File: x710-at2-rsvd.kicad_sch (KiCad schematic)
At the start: 37 parts, among them U1 EZX710AT2_S_LMR5

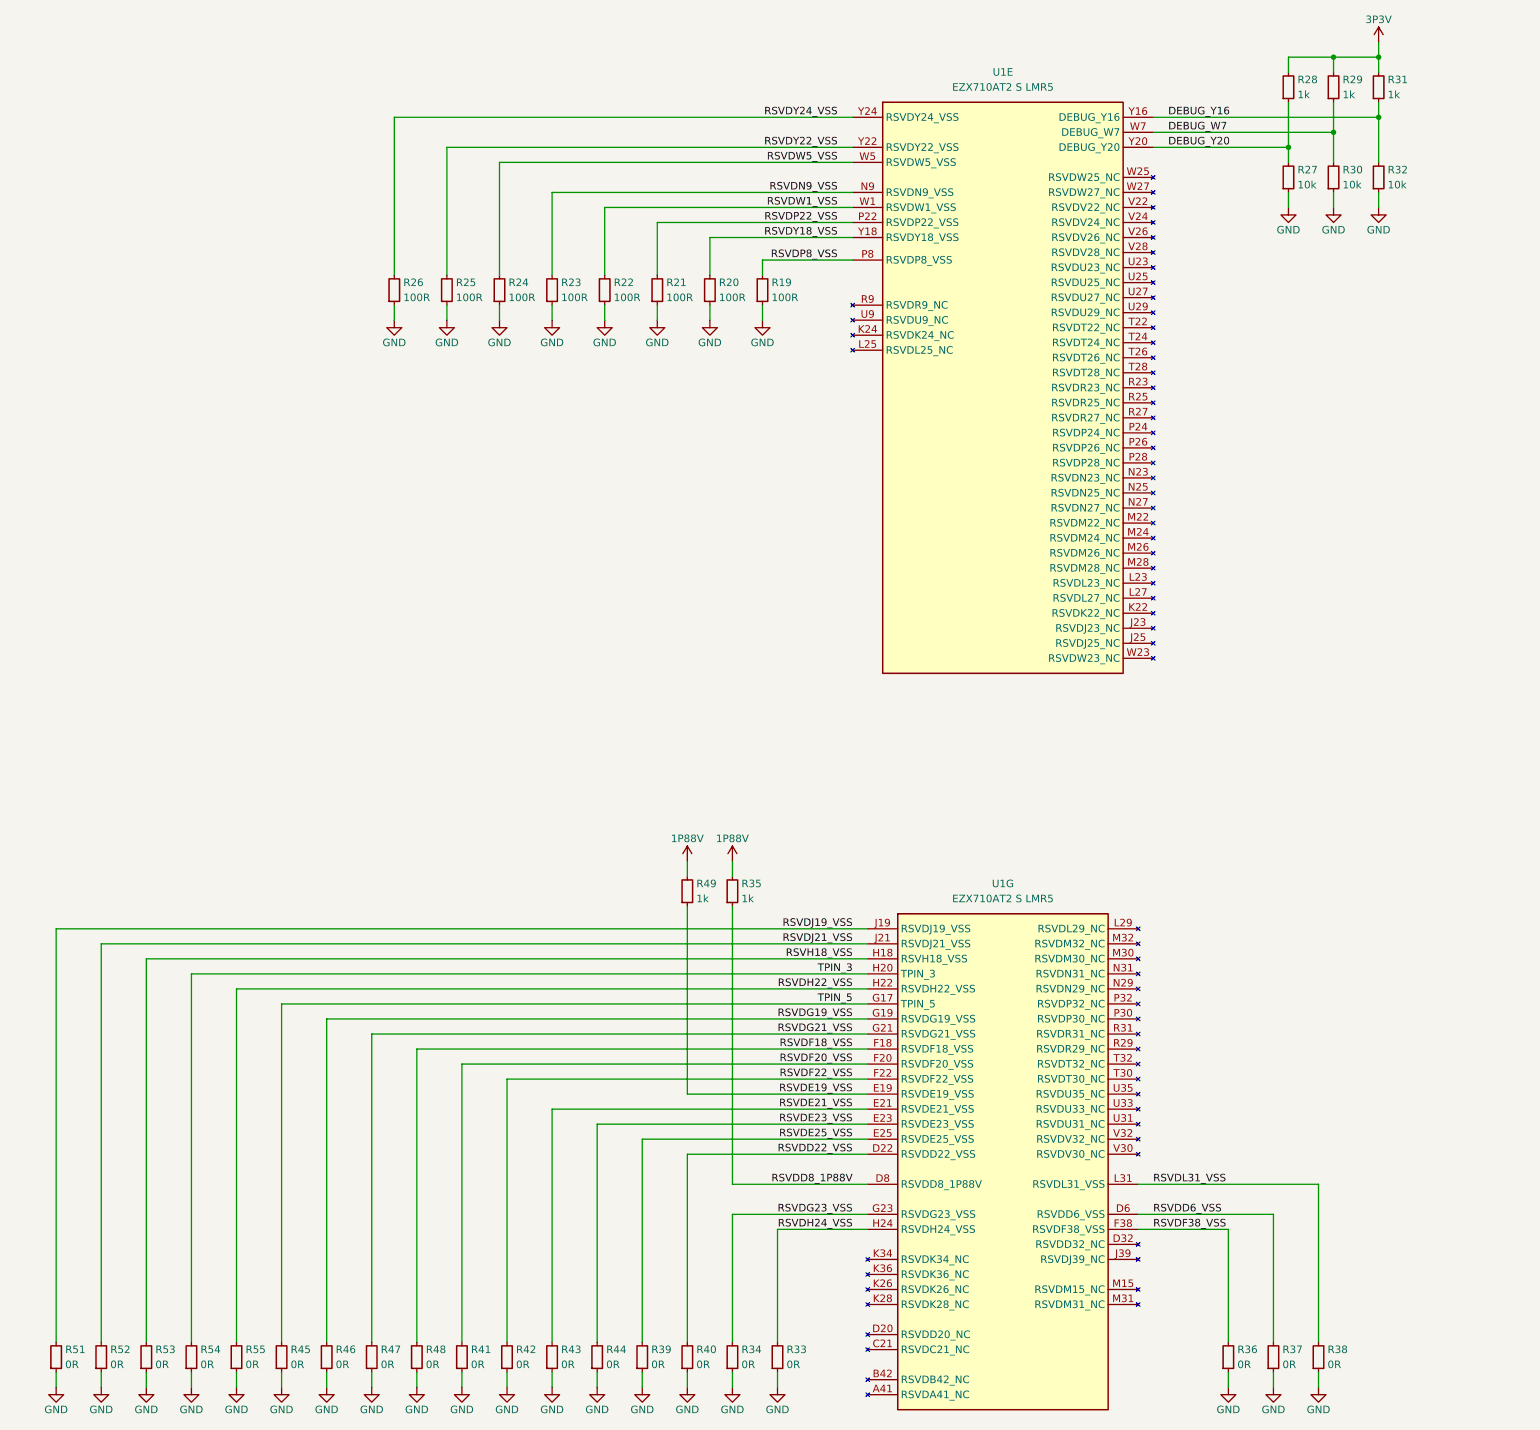
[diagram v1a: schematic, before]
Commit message: [#80813] Change RJ45 connectors, reannotate schematics
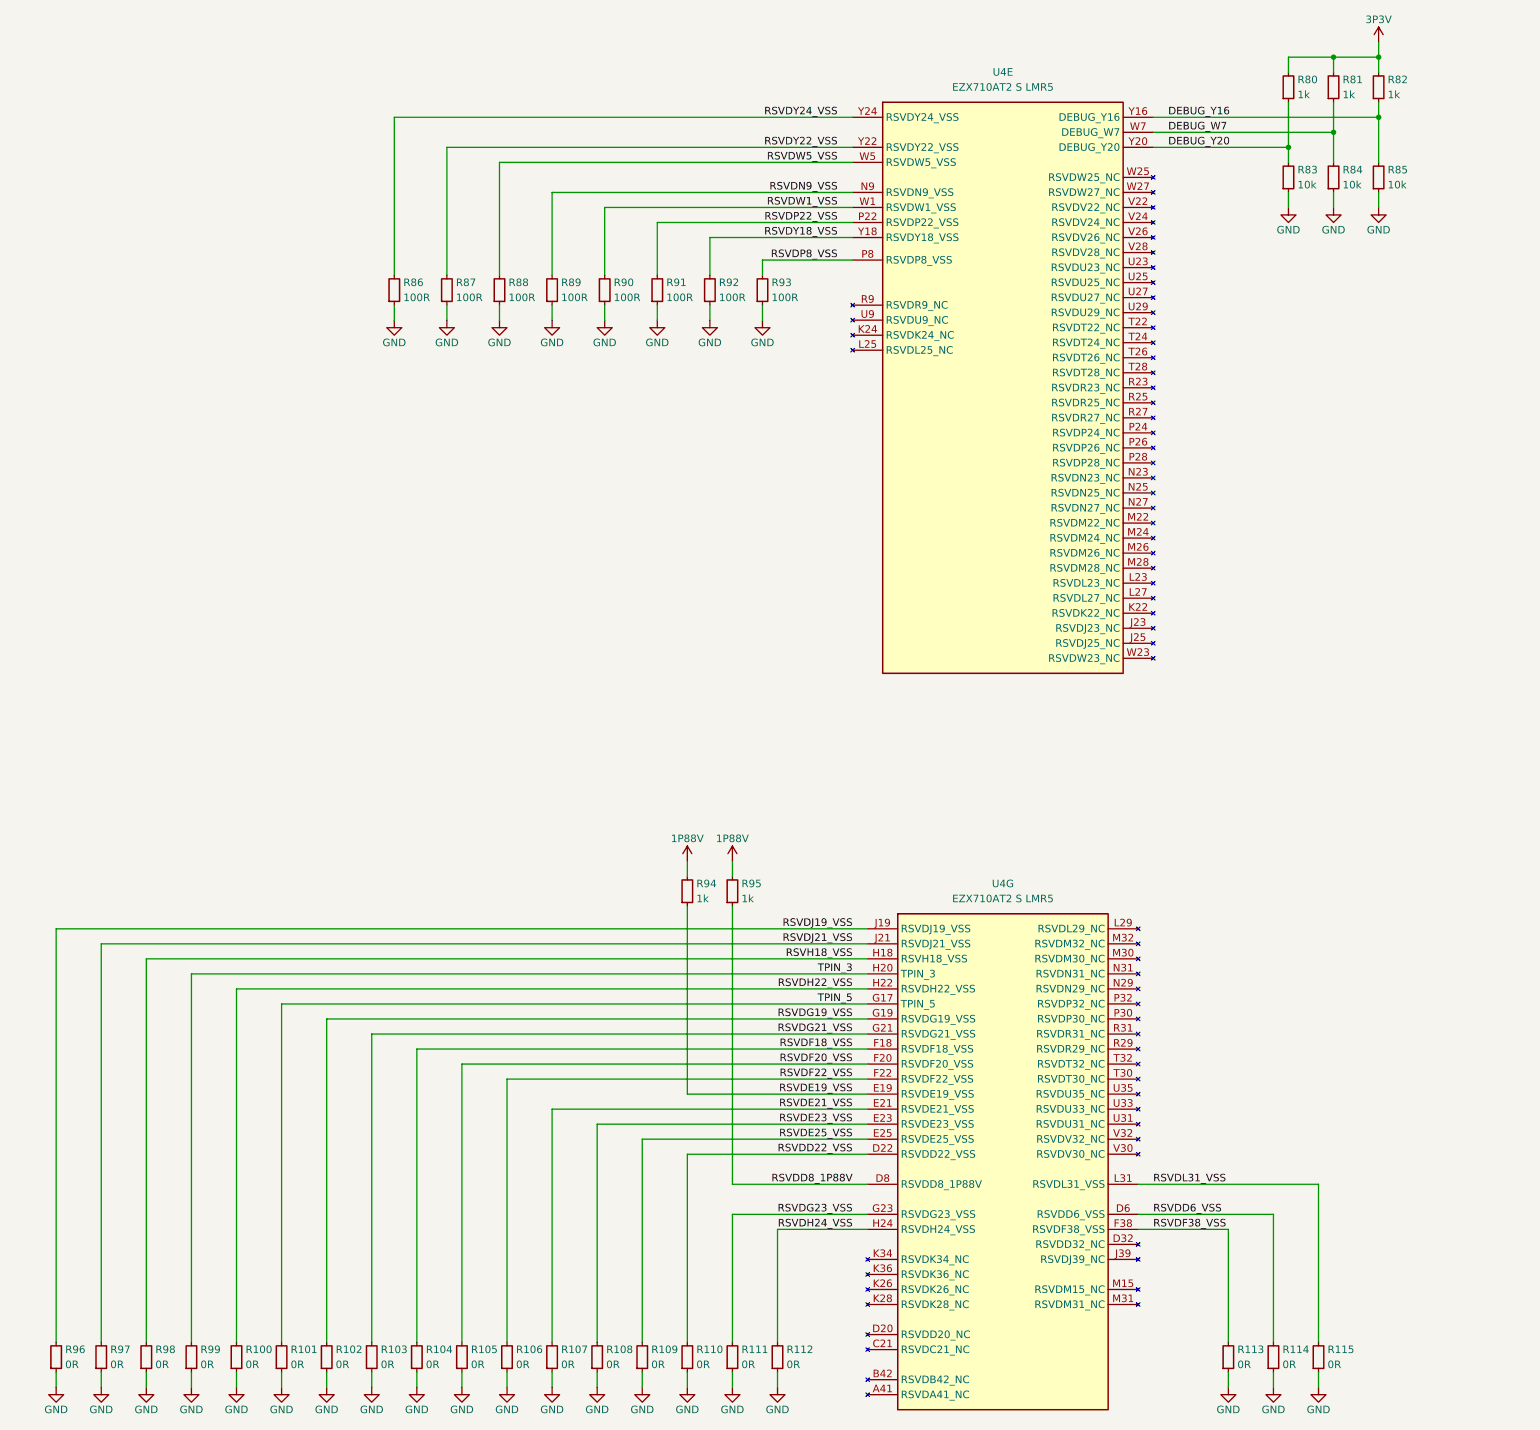
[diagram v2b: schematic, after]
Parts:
- renumbered R55 to R100, R45 to R101, R46 to R102, R47 to R103, R48 to R104, R41 to R105, R42 to R106, R43 to R107, R44 to R108, R39 to R109, R40 to R110, R34 to R111, R33 to R112, R36 to R113, R37 to R114, R38 to R115, R28 to R80, R29 to R81, R31 to R82, R27 to R83, R30 to R84, R32 to R85, R26 to R86, R25 to R87, R24 to R88, R23 to R89, R22 to R90, R21 to R91, R20 to R92, R19 to R93, R49 to R94, R35 to R95, R51 to R96, R52 to R97, R53 to R98, R54 to R99, U1 to U4

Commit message: [#80813] Improve schematic readability, add debug connectors and missing resistors
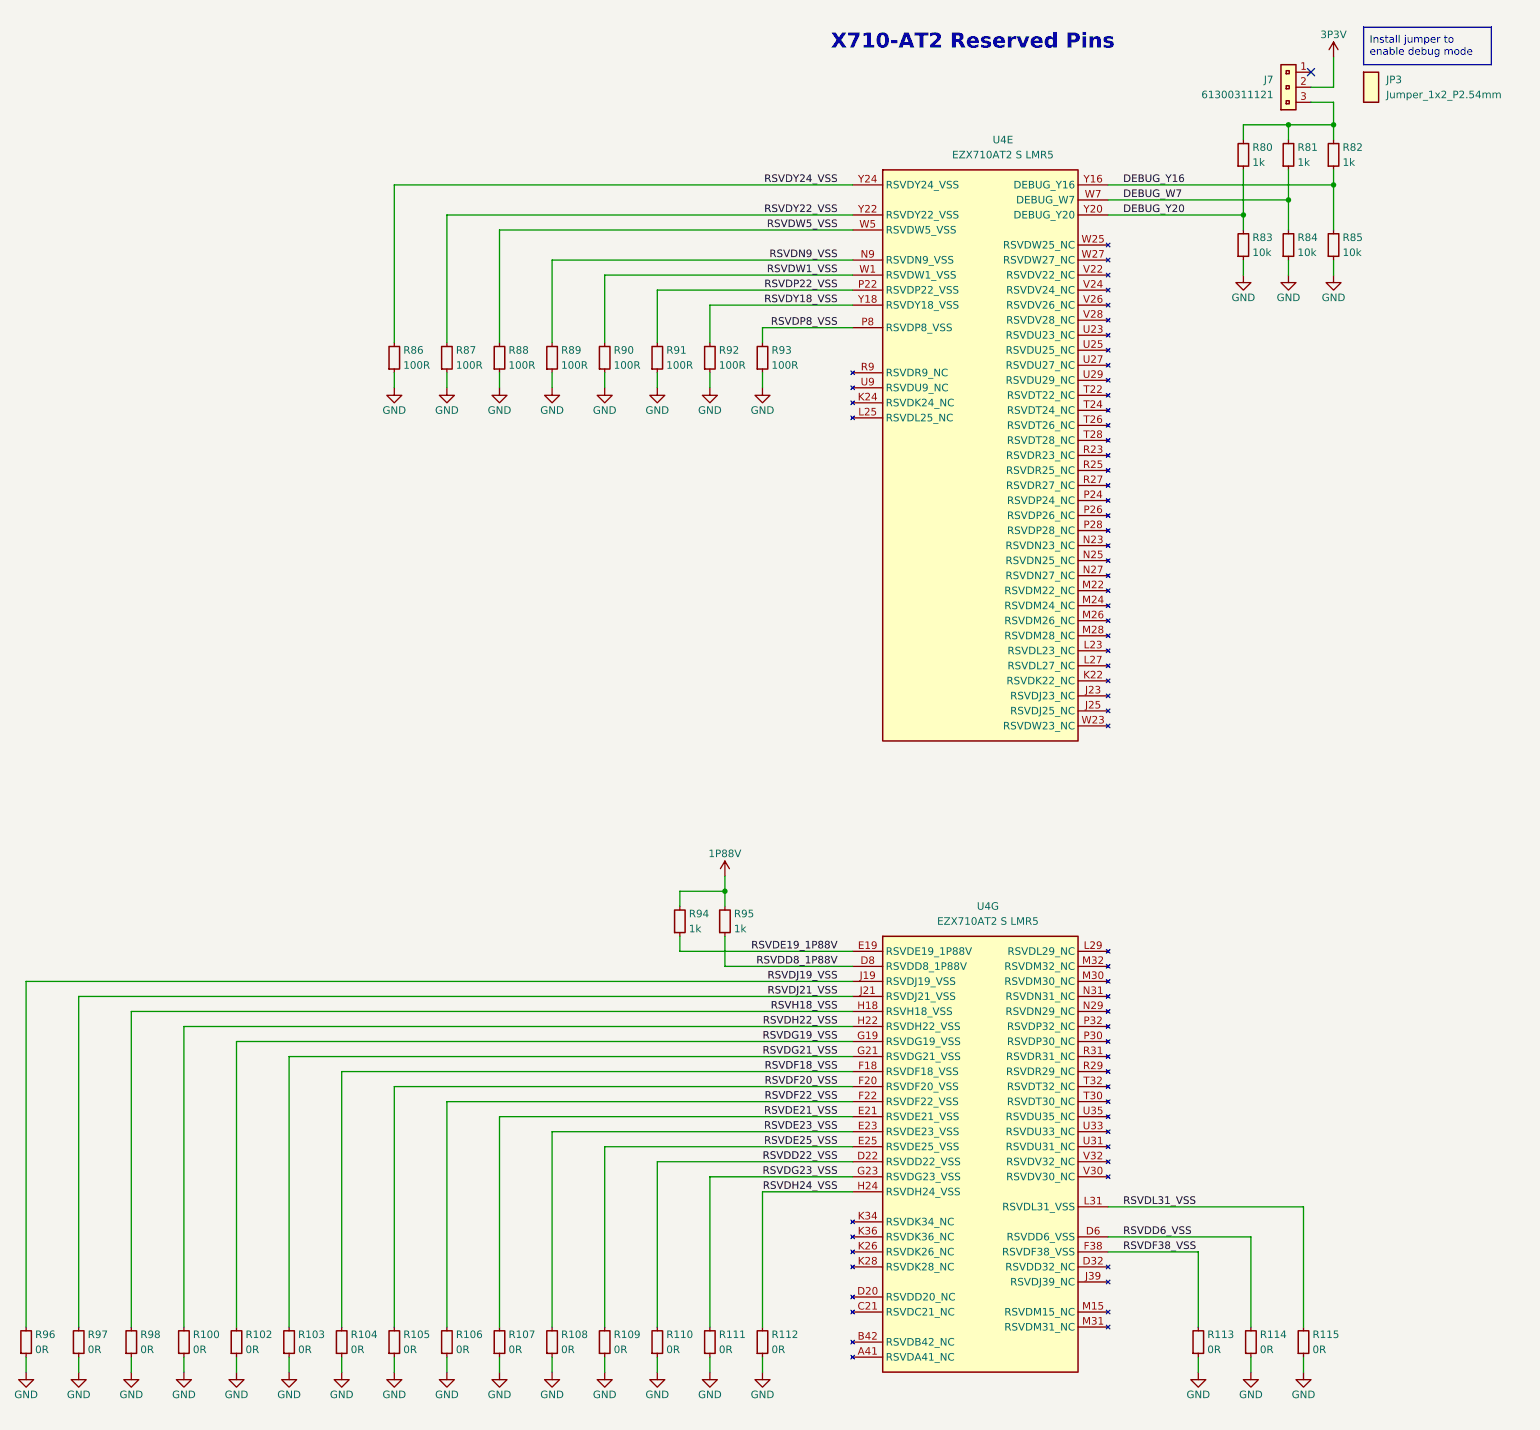
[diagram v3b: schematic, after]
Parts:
- removed R101, R99: R_0R_0402, antmicro-footprints:R_0402_1005Metric, symbol antmicroResistors0402:R_0R_0402
- added J7: PinHeader_1x3_P2.54mm_Drill1.1mm, antmicro-footprints:PinHeader_1x3_P2.54mm_Drill1.1mm, symbol antmicroGenericPinHeaders:PinHeader_1x3_P2.54mm_Drill1.1mm
- added JP3: Jumper_1x2_P2.54mm, antmicro-footprints:Jumper_1x2_P2.54mm, symbol antmicroShuntsJumpers:Jumper_1x2_P2.54mm
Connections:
- net 3P3V: now also J7.2; no longer R80.2, R81.2, R82.2
- net RSVDE19_VSS renamed RSVDE19_1P88V
- removed net TPIN_3: U4.H20 (TPIN_3)
- removed net TPIN_5: U4.G17 (TPIN_5)
- new net: J7.3, R80.2, R81.2, R82.2
- no-connect marks 0 -> 1
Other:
- note added: "Install jumper to enable debug mode"
- note added: "X710-AT2 Reserved Pins"
- moved on the sheet: R100, R102, R103, R104, R105, R106, R107, R108, R109, R110, R111, R112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
